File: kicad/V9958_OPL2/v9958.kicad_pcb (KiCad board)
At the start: 2 copper layers, 160 x 100.3 mm, 56 parts, among them P1 RED, P2 GREEN, P3 BLUE, P4 SYNC/C, P5 CONN_02X25, U1 74LS139, U2 V9958, U3 DRAM_64KX4, U4 DRAM_64KX4, U5 DRAM_64KX4, U6 DRAM_64KX4, U7 cxa2075M, U8 YM3812, U9 Y3014B, X1 OSC, X2 S-VIDEO, Y1 21,443Mhz

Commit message: stuff
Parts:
- removed JP1: JUMPER, Pin_Headers:Pin_Header_Straight_1x02
- removed P1: RED, w_conn_av:rca_black
- removed P2: GREEN, w_conn_av:rca_black
- removed P3: BLUE, w_conn_av:rca_black
- removed P4: SYNC/C, w_conn_av:rca_black
- removed X2: S-VIDEO, mini_din:mini_din-M_DIN4
- added C22: 220µF, Capacitors_ThroughHole:CP_Radial_D6.3mm_P2.50mm, F.Cu at (157.7, 165.2)
- added C23: 47µF, Capacitors_ThroughHole:CP_Radial_D6.3mm_P2.50mm, F.Cu at (134.9, 172.3)
- added C24: 220µF, Capacitors_ThroughHole:CP_Radial_D6.3mm_P2.50mm, F.Cu at (169.4, 174.4)
- added C25: 100n, Capacitors_ThroughHole:C_Disc_D3.0mm_W2.0mm_P2.50mm, F.Cu at (147.5, 123.7)
- added C26: 220µF, Capacitors_ThroughHole:CP_Radial_D6.3mm_P2.50mm, F.Cu at (135.5, 182.4)
- added C27: 220µF, Capacitors_ThroughHole:CP_Radial_D6.3mm_P2.50mm, F.Cu at (116.3, 175.1)
- added J1: Audio, w_conn_av:rca_black, F.Cu at (71.1, 127.0)
- added J2: RGB, w_conn_av:din-8, F.Cu at (71.1, 76.2)
- added J3: Composite, w_conn_av:rca_yellow, F.Cu at (71.1, 111.8)
- added J4: S-VIDEO, mini_din:mini_din-M_DIN4, F.Cu at (67.3, 95.2)
- added R14: 75, Discret:R3, F.Cu at (148.3, 190.1)
- added R15: 43, Discret:R3, F.Cu at (157.8, 198.2)
- added R16: 2.61k/10%, Discret:R3, F.Cu at (157.8, 187.5)
- added R17: 75, Discret:R3, F.Cu at (148.3, 187.5)
- added R18: 75, Discret:R3, F.Cu at (167.3, 187.5)
- added R19: 240, Discret:R3, F.Cu at (157.8, 195.5)
- added U10: Y3014B, Housings_DIP:DIP-8_W7.62mm_LongPads, F.Cu at (128.4, 126.1)
- added U11: LM324, Housings_DIP:DIP-14_W7.62mm_Socket_LongPads, F.Cu at (98.2, 116.3)
- added U12: cxa2075M, Housings_SOIC:SOIC-24W_7.5x15.4mm_Pitch1.27mm, F.Cu at (93.0, 91.8)
- C1, C10, C19, C2, C3, C4, C5, C6, C7, C8, C9: footprint Capacitors_ThroughHole:C_Disc_D3_P2.5 -> Capacitors_ThroughHole:C_Disc_D3.0mm_W1.6mm_P2.50mm
- C11: value 47µF -> 10µF; footprint Capacitors_ThroughHole:C_Radial_D5_L11_P2.5 -> Capacitors_ThroughHole:CP_Radial_D6.3mm_P2.50mm
- C12, C13: value 100n -> 470p; footprint Capacitors_ThroughHole:C_Disc_D3_P2.5 -> Capacitors_ThroughHole:C_Disc_D3.0mm_W1.6mm_P2.50mm
- C14: value 220µF -> 10µF; footprint Capacitors_ThroughHole:C_Radial_D6.3_L11.2_P2.5 -> Capacitors_ThroughHole:CP_Radial_D6.3mm_P2.50mm
- C15, C16, C18: value 220µF -> 100n; footprint Capacitors_ThroughHole:C_Radial_D6.3_L11.2_P2.5 -> Capacitors_ThroughHole:C_Disc_D3.0mm_W1.6mm_P2.50mm
- C17: footprint Capacitors_ThroughHole:C_Radial_D5_L11_P2.5 -> Capacitors_ThroughHole:CP_Radial_D6.3mm_P2.50mm
- C20, C21: footprint Capacitors_ThroughHole:C_Radial_D6.3_L11.2_P2.5 -> Capacitors_ThroughHole:CP_Radial_D6.3mm_P2.50mm
- R1, R3: value 470 -> 33K
- R10: value 2.61k/10% -> 2.2k
- R11: value 75 -> 2.2k
- R13: value 240 -> 75
- R2: value 470 -> 4K7
- R4: value 2.2k -> 15K
- R5: value 2.2k -> 27K
- R6: value 75 -> 4K7
- R7, R8: value 75 -> 470
- R9: value 43 -> 470
- U7: value cxa2075M -> DRAM_64KX4; footprint Housings_SOIC:SOIC-24_7.5x15.4mm_Pitch1.27mm -> Housings_DIP:DIP-18_W7.62mm_LongPads
- U9: value Y3014B -> DRAM_64KX4; footprint Housings_DIP:DIP-8_W7.62mm_LongPads -> Housings_DIP:DIP-18_W7.62mm_LongPads
- X1: footprint Oscillators:KXO-200_LargePads -> Oscillators:Oscillator_DIP-14_LargePads
- moved R6 184.6 mm to (251.1, 176.6), turned to 0 degrees
- moved R4 159.3 mm to (251.1, 179.2), turned to 0 degrees
- moved R11 157.4 mm to (198.7, 211.7), turned to 0 degrees
- moved R5 133.4 mm to (262.6, 168.9), turned to 0 degrees
- moved R7 130.1 mm to (181.2, 180.6), turned to 0 degrees
- moved R8 123.3 mm to (157.8, 192.8), turned to 0 degrees
- moved R9 121.0 mm to (148.3, 198.2), turned to 0 degrees
- moved C15 118.5 mm to (158.4, 155.6), turned to 0 degrees
- moved R13 114.0 mm to (148.3, 192.8), turned to 0 degrees
- moved C21 112.6 mm to (179.6, 160.8), turned to 0 degrees
- moved R12 112.0 mm to (148.3, 195.5), turned to 0 degrees
- moved C20 111.6 mm to (174.4, 154.1), turned to 0 degrees
- moved R1 107.1 mm to (273.8, 157.1), turned to 0 degrees
- moved R10 105.0 mm to (157.8, 190.1), turned to 0 degrees
- moved C19 103.2 mm to (167.6, 167.6), turned to 0 degrees
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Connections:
- C10 pad 1: /RGB_G -> VCC
- C10 pad 2: Net-(C10-Pad2) -> GND
- C11 pad 1: VCC -> Net-(C11-Pad1)
- C12 pad 1: /RGB_R -> GND
- C13 pad 1: VCC -> Net-(C13-Pad1)
- C13 pad 2: GND -> Net-(C13-Pad2)
- C14 pad 2: /C_OUT -> /Audio/AUDIO_OUT
- C15 pad 1: Net-(C15-Pad1) -> /RGB_B
- C16 pad 1: Net-(C16-Pad1) -> /RGB_G
- C16 pad 2: /Y_OUT -> Net-(C16-Pad2)
- C18 pad 1: Net-(C18-Pad1) -> /RGB_R
- C20 pad 2: Net-(C20-Pad2) -> /Video/C_OUT
- C9 pad 1: /RGB_B -> VCC
- C9 pad 2: Net-(C9-Pad2) -> GND
- R1 pad 1: GND -> Net-(R1-Pad1)
- R1 pad 2: /RGB_G -> Net-(C13-Pad2)
- R10 pad 2: VCC -> Net-(R10-Pad2)
- R11 pad 1: Net-(R11-Pad1) -> /CSYNC
- R11 pad 2: Net-(C16-Pad1) -> Net-(R11-Pad2)
- R12 pad 2: Net-(C14-Pad1) -> Net-(C21-Pad1)
- R13 pad 1: Net-(C21-Pad1) -> Net-(R13-Pad1)
- R13 pad 2: GND -> Net-(C24-Pad1)
- R2 pad 2: /RGB_R -> Net-(R2-Pad2)
- R3 pad 1: GND -> Net-(C13-Pad2)
- R3 pad 2: /RGB_B -> Net-(C12-Pad2)
- R4 pad 1: Net-(R4-Pad1) -> Net-(R2-Pad2)
- R5 pad 1: /CSYNC -> Net-(R4-Pad2)
- R5 pad 2: Net-(R5-Pad2) -> Net-(C14-Pad1)
- R6 pad 1: Net-(R6-Pad1) -> GND
- R6 pad 2: Net-(C15-Pad1) -> Net-(C14-Pad1)
- R7 pad 1: Net-(R7-Pad1) -> GND
- R7 pad 2: Net-(C18-Pad1) -> /RGB_G
- R8 pad 1: Net-(R8-Pad1) -> GND
- R8 pad 2: Net-(C20-Pad1) -> /RGB_R
- R9 pad 1: Net-(R9-Pad1) -> GND
- R9 pad 2: Net-(C21-Pad1) -> /RGB_B
- U2 pad 59: Net-(U2-Pad59) -> //CAS_X
- U7 pad 10: Net-(R5-Pad2) -> /AD7
- U7 pad 11: (no net) -> /AD3
- U7 pad 12: VCC -> /AD2
- U7 pad 13: (no net) -> /AD1
- U7 pad 14: (no net) -> /AD0
- U7 pad 15: Net-(R12-Pad1) -> /RD2
- U7 pad 16: Net-(R11-Pad1) -> //CAS_X
- U7 pad 17: Net-(R10-Pad1) -> /RD3
- U7 pad 18: (no net) -> GND
- U7 pad 2: Net-(C12-Pad2) -> /RD0
- U7 pad 3: Net-(C10-Pad2) -> /RD1
- U7 pad 4: Net-(C9-Pad2) -> /R/W
- U7 pad 5: (no net) -> //RAS
- U7 pad 6: Net-(R4-Pad2) -> /AD6
- U7 pad 7: GND -> /AD5
- U7 pad 8: Net-(U7-Pad8) -> /AD4
- U7 pad 9: (no net) -> VCC
- U8 pad 20: Net-(U8-Pad20) -> /Audio/LOAD
- U8 pad 21: Net-(U8-Pad21) -> /Audio/SD
- U8 pad 23: Net-(U8-Pad23) -> /Audio/fl
- U9 pad 1: VCC -> GND
- U9 pad 2: Net-(U9-Pad2) -> /RD4
- U9 pad 3: Net-(U8-Pad20) -> /RD5
- U9 pad 4: Net-(U8-Pad21) -> /R/W
- U9 pad 5: Net-(U8-Pad23) -> //RAS
- U9 pad 6: GND -> /AD6
- U9 pad 7: Net-(U9-Pad7) -> /AD5
- U9 pad 8: Net-(U9-Pad8) -> /AD4
- X1 pad 8: Net-(R4-Pad1) -> Net-(R10-Pad1)
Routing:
- net GND: track 411.7 -> 210.2 mm, vias 1 -> 0
- net /IRQ: track 82.1 -> 0.00 mm, vias 1 -> 0
- net Net-(C9-Pad2): track 75.5 -> 0.00 mm
- net Net-(C12-Pad2): track 73.2 -> 0.00 mm
- net Net-(C10-Pad2): track 71.5 -> 0.00 mm
- net /AD6: track 69.2 -> 0.00 mm
- net //RAS: track 62.6 -> 0.00 mm
- net /RD6: track 60.7 -> 0.00 mm, vias 1 -> 0
- net /R/W: track 60.7 -> 0.00 mm
- net /RD5: track 56.4 -> 0.00 mm, vias 1 -> 0
- net /RD7: track 54.2 -> 0.00 mm
- net /RESET: track 111.0 -> 161.6 mm, vias 1 -> 0
- net /RD4: track 50.5 -> 0.00 mm
- net Net-(JP1-Pad2): track 46.8 -> 0.00 mm
- net /AD3: track 42.0 -> 0.00 mm
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- removed copper zone on F.Cu, net GND
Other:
- board text removed: "Steckschwein V9958/Video Board v0.1 2018 Thomas Woinke / Marko Lauke http://www.steckschwein.de/"

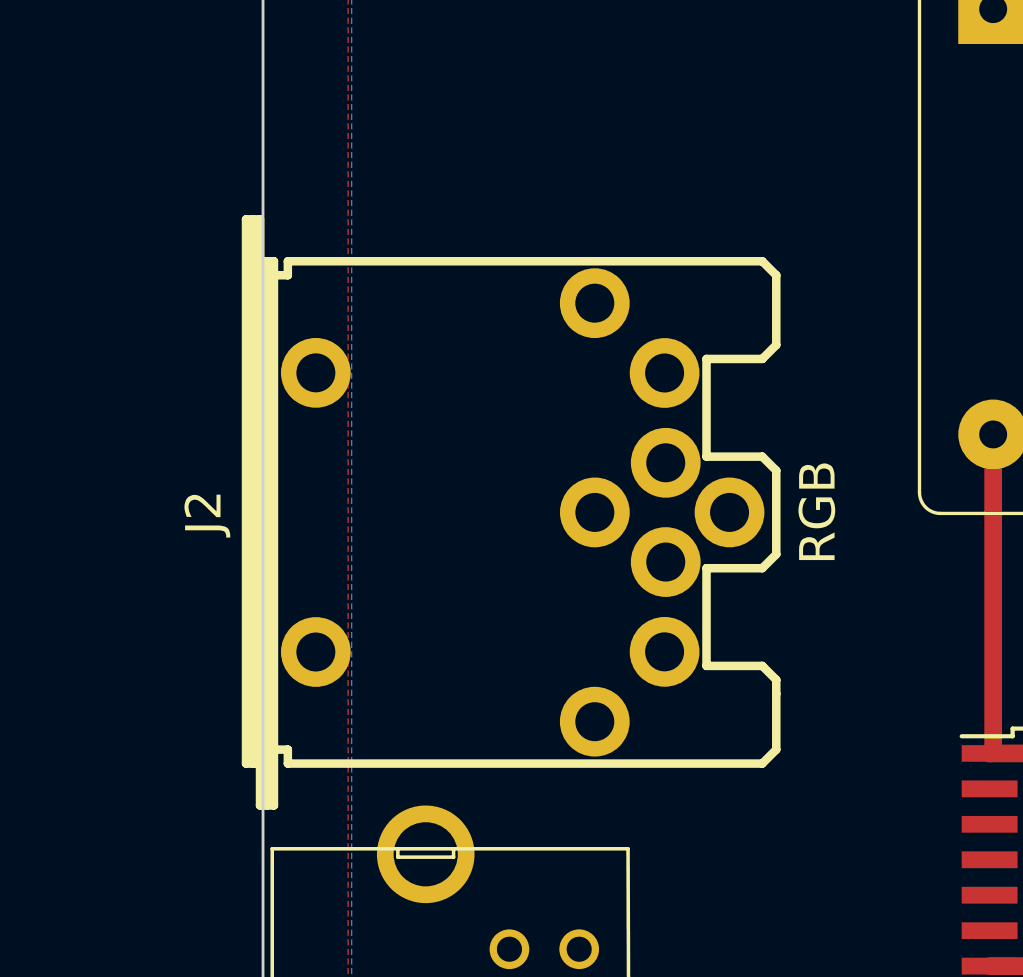
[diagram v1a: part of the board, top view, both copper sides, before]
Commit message: din 8 jack footprint
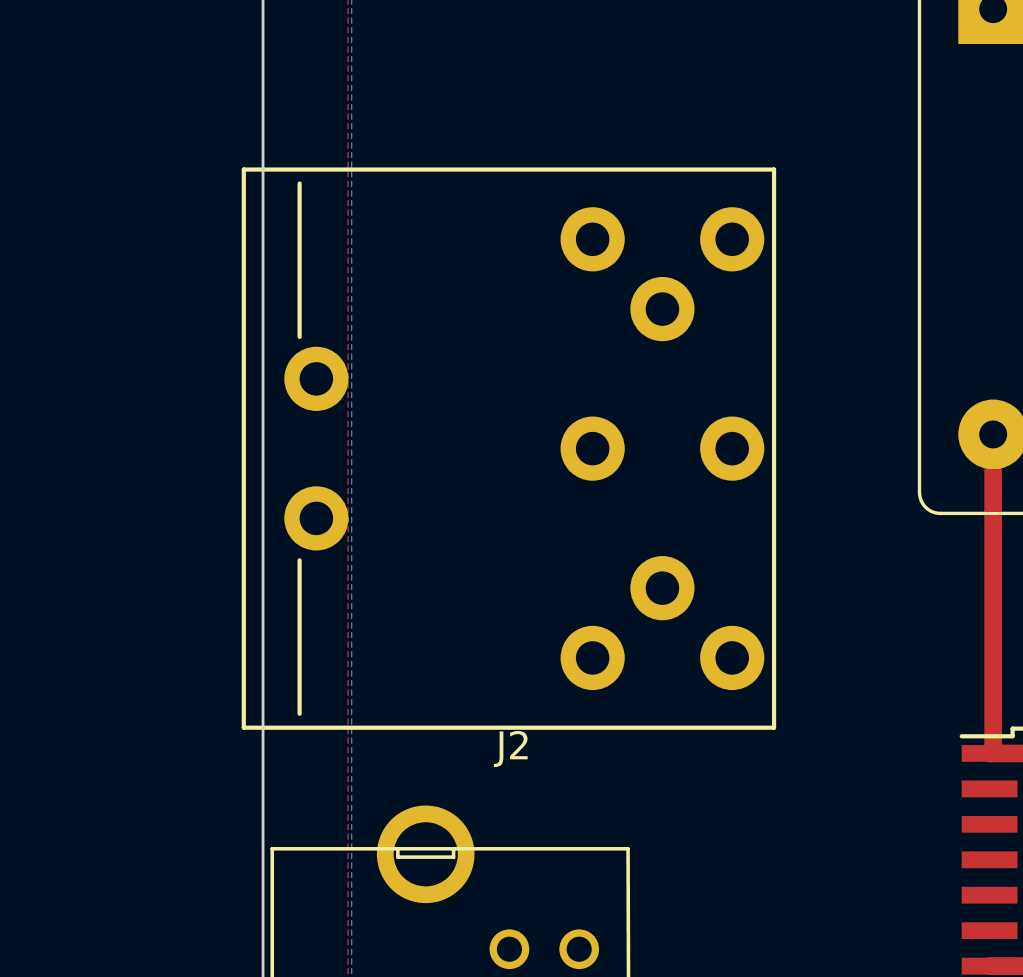
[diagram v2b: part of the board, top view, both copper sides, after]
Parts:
- J2: footprint w_conn_av:din-8 -> w_conn_av:DIN-8
- moved J2 3.71 mm to (74.0, 73.9), turned to 90 degrees
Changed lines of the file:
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@@
   (general
     (links 281)
-    (no_connects 280)
+    (no_connects 222)
     (area 62.179999 45.669999 222.300001 146.100001)
     (thickness 1.6)
@@
     )
   )
-  (module w_conn_av:din-8 (layer F.Cu)
-    (at 71.12 76.2 270)
-    (descr "Din 5 (MIDI), Pro Signal P/N PSG03463")
-    (fp_text reference J2 (at 0 11.00074 270) (layer F.SilkS)
-      (effects (font (thickness 0.3048)))
-    )
-    (fp_text value RGB (at 0 -11.00074 270) (layer F.SilkS)
-      (effects (font (thickness 0.3048)))
-    )
-    (fp_line (start -8.99922 8.7503) (end 10.50036 8.7503) (layer F.SilkS) (width 0.3048))
-    (fp_line (start 8.99922 8.99922) (end -8.99922 8.99922) (layer F.SilkS) (width 0.3048))
-    (fp_line (start -10.50036 9.25068) (end 8.99922 9.25068) (layer F.SilkS) (width 0.3048))
-    (fp_line (start -8.99922 -8.99922) (end -8.99922 8.001) (layer F.SilkS) (width 0.3048))
-    (fp_line (start -8.99922 -8.99922) (end -8.49884 -9.4996) (layer F.SilkS) (width 0.3048))
-    (fp_line (start -8.49884 -9.4996) (end -5.99948 -9.4996) (layer F.SilkS) (width 0.3048))
-    (fp_line (start -5.99948 -9.4996) (end -5.4991 -8.99922) (layer F.SilkS) (width 0.3048))
-    (fp_line (start -5.4991 -8.99922) (end -5.4991 -7.00024) (layer F.SilkS) (width 0.3048))
-    (fp_line (start -5.4991 -7.00024) (end -1.99898 -7.00024) (layer F.SilkS) (width 0.3048))
-    (fp_line (start 8.99922 -8.99922) (end 8.99922 8.001) (layer F.SilkS) (width 0.3048))
-    (fp_line (start 8.99922 -8.99922) (end 8.49884 -9.4996) (layer F.SilkS) (width 0.3048))
-    (fp_line (start 8.49884 -9.4996) (end 6.49986 -9.4996) (layer F.SilkS) (width 0.3048))
-    (fp_line (start 6.49986 -9.4996) (end 5.99948 -9.4996) (layer F.SilkS) (width 0.3048))
-    (fp_line (start 5.99948 -9.4996) (end 5.4991 -8.99922) (layer F.SilkS) (width 0.3048))
-    (fp_line (start 5.4991 -8.99922) (end 5.4991 -7.00024) (layer F.SilkS) (width 0.3048))
-    (fp_line (start 5.4991 -7.00024) (end 1.99898 -7.00024) (layer F.SilkS) (width 0.3048))
-    (fp_line (start -1.50114 -9.4996) (end -1.99898 -8.99922) (layer F.SilkS) (width 0.3048))
-    (fp_line (start -1.99898 -8.99922) (end -1.99898 -7.00024) (layer F.SilkS) (width 0.3048))
-    (fp_line (start -1.50114 -9.4996) (end 1.50114 -9.4996) (layer F.SilkS) (width 0.3048))
-    (fp_line (start 1.50114 -9.4996) (end 1.99898 -8.99922) (layer F.SilkS) (width 0.3048))
-    (fp_line (start 1.99898 -8.99922) (end 1.99898 -7.00024) (layer F.SilkS) (width 0.3048))
-    (fp_line (start 10.50036 8.99922) (end 8.99922 8.99922) (layer F.SilkS) (width 0.3048))
-    (fp_line (start 8.99922 8.99922) (end 8.99922 9.4996) (layer F.SilkS) (width 0.3048))
-    (fp_line (start 8.99922 9.4996) (end -10.50036 9.4996) (layer F.SilkS) (width 0.3048))
-    (fp_line (start -10.50036 8.99922) (end -8.99922 8.99922) (layer F.SilkS) (width 0.3048))
-    (fp_line (start -8.99922 8.99922) (end -8.99922 8.49884) (layer F.SilkS) (width 0.3048))
-    (fp_line (start -8.99922 8.49884) (end 10.50036 8.49884) (layer F.SilkS) (width 0.3048))
-    (fp_line (start 8.99922 8.001) (end 8.49884 8.001) (layer F.SilkS) (width 0.3048))
-    (fp_line (start -8.99922 8.001) (end -8.49884 8.001) (layer F.SilkS) (width 0.3048))
-    (fp_line (start 8.49884 8.49884) (end 8.49884 8.001) (layer F.SilkS) (width 0.3048))
-    (fp_line (start -8.49884 8.001) (end -8.49884 8.49884) (layer F.SilkS) (width 0.3048))
-    (fp_line (start -10.50036 9.4996) (end -10.50036 8.99922) (layer F.SilkS) (width 0.3048))
-    (fp_line (start 10.50036 8.49884) (end 10.50036 8.99922) (layer F.SilkS) (width 0.3048))
-    (pad 8 thru_hole circle (at 0 -7.82574 270) (size 2.49936 2.49936) (drill 1.397) (layers *.Cu *.SilkS *.Mask)
-      (net 121 /Video/B_OUT))
-    (pad 7 thru_hole circle (at 1.778 -5.53974 270) (size 2.49936 2.49936) (drill 1.397) (layers *.Cu *.SilkS *.Mask)
+  (module w_conn_av:DIN-8 (layer F.Cu)
+    (at 74.041 73.914 90)
+    (fp_text reference J2 (at -10.67 -2.83 360) (layer F.SilkS)
+      (effects (font (size 1 1) (thickness 0.15)))
+    )
+    (fp_text value RGB (at 0 -8 90) (layer F.SilkS) hide
+      (effects (font (size 1 1) (thickness 0.15)))
+    )
+    (fp_line (start 10 6.5) (end 10 -12.5) (layer F.SilkS) (width 0.15))
+    (fp_line (start -10 6.5) (end 10 6.5) (layer F.SilkS) (width 0.15))
+    (fp_line (start -10 -12.5) (end -10 6.5) (layer F.SilkS) (width 0.15))
+    (fp_line (start 10 -12.5) (end -10 -12.5) (layer F.SilkS) (width 0.15))
+    (fp_line (start -9.5 -10.5) (end -4 -10.5) (layer F.SilkS) (width 0.15))
+    (fp_line (start 4 -10.5) (end 9.5 -10.5) (layer F.SilkS) (width 0.15))
+    (pad "" thru_hole circle (at -2.5 -9.9 90) (size 2.3 2.3) (drill 1.2) (layers *.Cu *.Mask))
+    (pad "" thru_hole circle (at 2.5 -9.9 90) (size 2.3 2.3) (drill 1.2) (layers *.Cu *.Mask))
+    (pad 5 thru_hole circle (at 5 2.5 90) (size 2.3 2.3) (drill 1.2) (layers *.Cu *.Mask)
+      (net 119 /Video/G_OUT))
+    (pad 4 thru_hole circle (at -5 2.5 90) (size 2.3 2.3) (drill 1.2) (layers *.Cu *.Mask)
+      (net 2 VCC))
+    (pad 7 thru_hole circle (at 7.5 5 90) (size 2.3 2.3) (drill 1.2) (layers *.Cu *.Mask)
       (net 118 /Video/CV_OUT))
-    (pad 6 thru_hole circle (at -1.778 -5.53974 270) (size 2.49936 2.49936) (drill 1.397) (layers *.Cu *.SilkS *.Mask)
+    (pad 6 thru_hole circle (at -7.5 5 90) (size 2.3 2.3) (drill 1.2) (layers *.Cu *.Mask)
       (net 122 /Video/R_OUT))
-    (pad 3 thru_hole circle (at -7.49808 -2.9972 270) (size 2.49936 2.49936) (drill 1.397) (layers *.Cu *.SilkS *.Mask)
+    (pad 3 thru_hole circle (at 7.5 0 90) (size 2.3 2.3) (drill 1.2) (layers *.Cu *.Mask)
       (net 118 /Video/CV_OUT))
-    (pad 4 thru_hole circle (at 4.99618 -5.4991 270) (size 2.49936 2.49936) (drill 1.397) (layers *.Cu *.SilkS *.Mask)
-      (net 2 VCC))
-    (pad 2 thru_hole circle (at 0 -2.99974 270) (size 2.49936 2.49936) (drill 1.397) (layers *.Cu *.SilkS *.Mask)
+    (pad 2 thru_hole circle (at 0 0 90) (size 2.3 2.3) (drill 1.2) (layers *.Cu *.Mask)
       (net 1 GND))
-    (pad 1 thru_hole circle (at 7.49808 -2.9972 270) (size 2.49936 2.49936) (drill 1.397) (layers *.Cu *.SilkS *.Mask)
+    (pad 1 thru_hole circle (at -7.5 0 90) (size 2.3 2.3) (drill 1.2) (layers *.Cu *.Mask)
       (net 117 /Audio/AUDIO_OUT))
-    (pad 5 thru_hole circle (at -4.99618 -5.4991 270) (size 2.49936 2.49936) (drill 1.397) (layers *.Cu *.SilkS *.Mask)
-      (net 119 /Video/G_OUT))
-    (pad "" np_thru_hole circle (at 5.00126 6.9977 270) (size 2.49936 2.49936) (drill 1.397) (layers *.Cu *.Mask F.SilkS))
-    (pad "" np_thru_hole circle (at -5.00126 6.9977 270) (size 2.49936 2.49936) (drill 1.397) (layers *.Cu *.Mask F.SilkS))
-    (model walter/conn_av/din-5.wrl
-      (at (xyz 0 0 0))
-      (scale (xyz 1 1 1))
-      (rotate (xyz 0 0 0))
-    )
+    (pad 8 thru_hole circle (at 0 5 90) (size 2.3 2.3) (drill 1.2) (layers *.Cu *.Mask)
+      (net 121 /Video/B_OUT))
   )
   (gr_line (start 62.23 146.05) (end 62.23 45.72) (angle 90) (layer Edge.Cuts) (width 0.1))

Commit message: layout almost done
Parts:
- moved R1 175.9 mm to (98.8, 138.7), turned to 270 degrees
- moved R5 171.5 mm to (98.8, 118.1), turned to 270 degrees
- moved R3 168.7 mm to (109.0, 118.1), turned to 270 degrees
- moved R4 161.7 mm to (101.3, 118.1), turned to 270 degrees
- moved R6 156.0 mm to (106.4, 118.1), turned to 90 degrees
- moved R2 153.8 mm to (111.5, 138.9), turned to 90 degrees
- moved R11 139.5 mm to (118.1, 97.8), turned to 90 degrees
- moved C24 128.4 mm to (91.5, 72.4)
- moved C21 125.4 mm to (105.4, 59.7)
- moved C20 122.8 mm to (83.8, 71.1), turned to 180 degrees
- moved C9 118.2 mm to (198.1, 63.5), turned to 90 degrees
- moved R18 117.3 mm to (96.5, 94.0), turned to 180 degrees
- moved C27 116.6 mm to (92.8, 61.0)
- moved R15 114.4 mm to (96.5, 101.6), turned to 180 degrees
- moved C22 113.8 mm to (83.8, 78.7), turned to 180 degrees
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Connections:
- U1 pad 1: /CS_VDP -> /CS_IO0
- U1 pad 11: //CSR_OPL3 -> Net-(U1-Pad11)
- U1 pad 12: //CSW_OPL3 -> Net-(U1-Pad12)
- U1 pad 15: /CS_IO0 -> /CS_VDP
- U1 pad 4: Net-(U1-Pad4) -> //CSW_OPL3
- U1 pad 5: Net-(U1-Pad5) -> //CSR_OPL3
- U2 pad 30: Net-(U1-Pad4) -> Net-(U1-Pad12)
- U2 pad 31: Net-(U1-Pad5) -> Net-(U1-Pad11)
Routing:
- net GND: track 210.2 -> 362.4 mm
- net /CS_IO0: track 0.00 -> 120.2 mm
- net /RW: track 0.00 -> 117.6 mm, vias 0 -> 1
- net /AD0: track 0.00 -> 109.2 mm, vias 0 -> 2
- net /CS_VDP: track 0.00 -> 104.9 mm, vias 0 -> 1
- net //RAS: track 0.00 -> 103.1 mm
- net /AD3: track 0.00 -> 99.5 mm, vias 0 -> 3
- net /AD1: track 0.00 -> 97.3 mm, vias 0 -> 1
- net /IRQ: track 0.00 -> 97.0 mm
- net /AD2: track 0.00 -> 95.2 mm, vias 0 -> 2
- net /R/W: track 0.00 -> 91.7 mm
- net /AD4: track 0.00 -> 91.3 mm, vias 0 -> 2
- net /AD6: track 0.00 -> 88.9 mm, vias 0 -> 2
- net /AD5: track 0.00 -> 88.6 mm, vias 0 -> 2
- net /RD0: track 0.00 -> 75.7 mm, vias 0 -> 1
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
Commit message: DRC fixes
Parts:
- moved C21 53.4 mm to (88.9, 110.5), turned to 180 degrees
- moved C23 29.1 mm to (113.1, 113.0), turned to 0 degrees
- moved C27 27.0 mm to (88.9, 87.6), turned to 180 degrees
- moved C24 23.0 mm to (88.9, 95.2), turned to 180 degrees
- moved C26 10.9 mm to (88.9, 102.9), turned to 180 degrees
- moved C22 5.12 mm to (88.9, 78.7)
- moved C20 5.08 mm to (88.9, 71.1)
- moved R17 3.81 mm to (96.5, 92.7), turned to 90 degrees
- moved R18 2.84 mm to (99.1, 92.7), turned to 90 degrees
- moved R11 2.84 mm to (115.6, 99.1)
- moved R10 2.54 mm to (118.1, 97.8)
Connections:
- C24 pad 2: Net-(C24-Pad2) -> /Video/G_OUT
- J2 pad 3: /Video/CV_OUT -> Net-(C27-Pad2)
- J2 pad 6: /Video/R_OUT -> Net-(C21-Pad2)
- J2 pad 7: /Video/CV_OUT -> Net-(C27-Pad2)
- J2 pad 8: /Video/B_OUT -> Net-(C26-Pad2)
- J3 pad 1: /Video/CV_OUT -> Net-(C27-Pad2)
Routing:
- net GND: track 362.4 -> 583.3 mm, vias 0 -> 1
- net VCC: track 278.8 -> 412.9 mm, vias 3 -> 5
- net Net-(C27-Pad2): track 0.00 -> 39.3 mm
- net /CSYNC: track 0.00 -> 38.6 mm
- net //CAS0: track 19.6 -> 53.7 mm, vias 1 -> 3
- net //CAS1: track 31.7 -> 61.8 mm, vias 1 -> 2
- net //CAS_X: track 43.7 -> 71.7 mm
- net Net-(C27-Pad1): track 0.00 -> 27.5 mm
- net /Audio/AUDIO_OUT: track 15.3 -> 41.1 mm
- net Net-(C20-Pad1): track 0.00 -> 22.6 mm
- net Net-(C24-Pad1): track 0.00 -> 15.3 mm
- net Net-(C22-Pad1): track 0.00 -> 13.9 mm
- net /Video/Y_OUT: track 0.00 -> 13.1 mm
- net /Video/C_OUT: track 0.00 -> 13.0 mm
- net /Video/G_OUT: track 0.00 -> 11.0 mm
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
